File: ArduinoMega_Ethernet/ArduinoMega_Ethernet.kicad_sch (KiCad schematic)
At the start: 17 parts, among them SW1 RST_BTN, U1 ATmega2560-16A, Y1 16Mhz

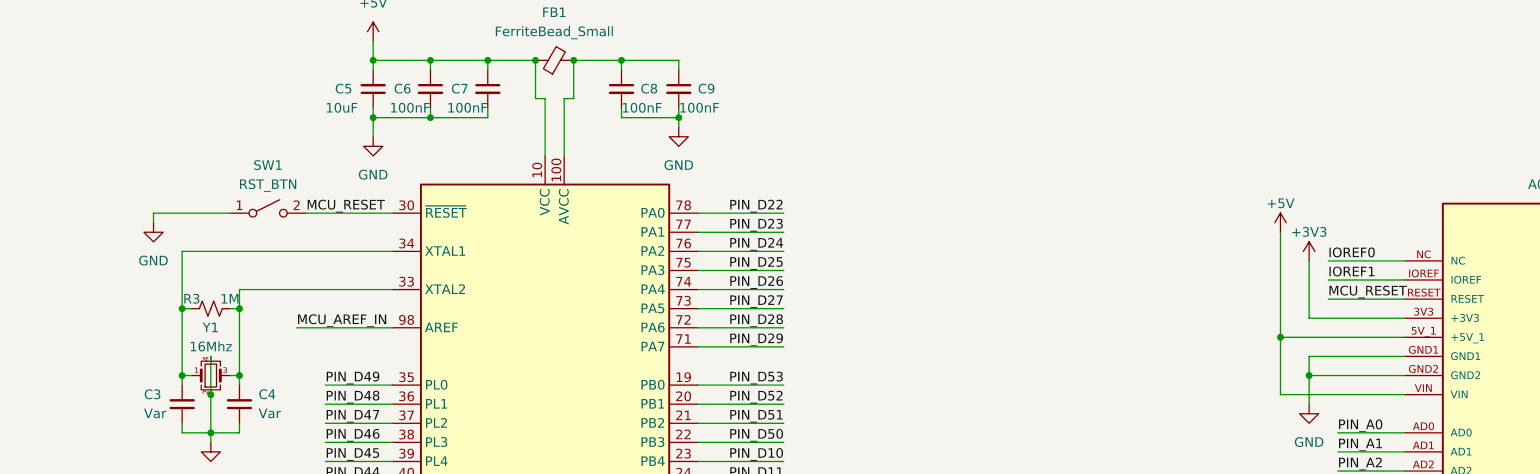
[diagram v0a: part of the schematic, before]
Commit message: add usb protection, fix ioref
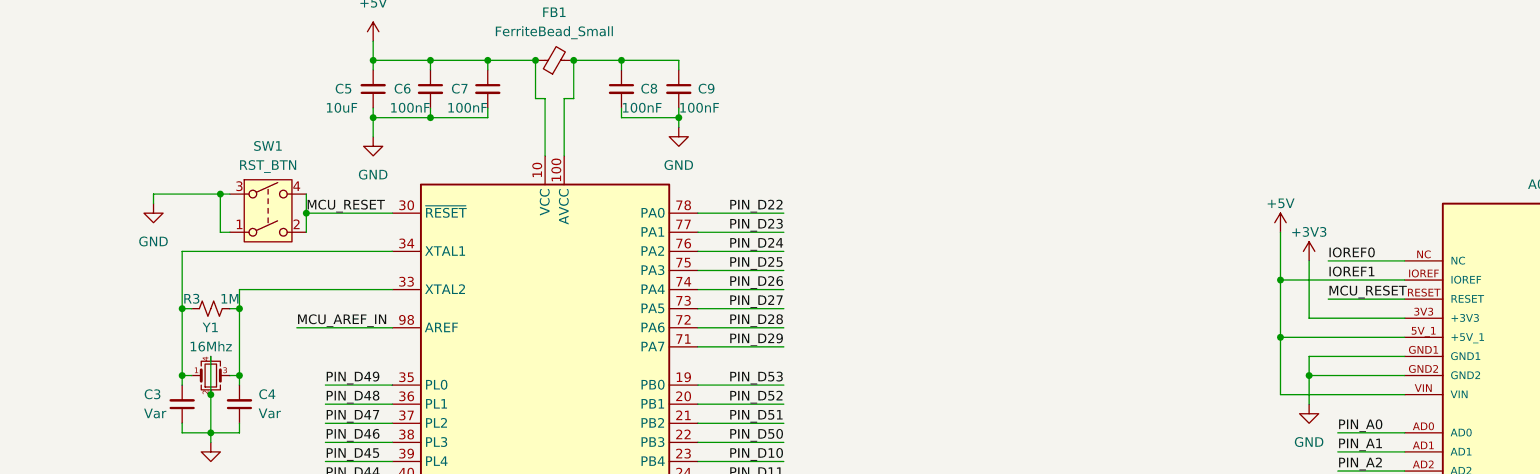
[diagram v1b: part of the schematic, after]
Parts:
- SW1: footprint Button_Switch_SMD:SW_Push_1P1T-MP_NO_Horizontal_Alps_SKRTLAE010 -> Button_Switch_SMD:SW_SPST_PTS645; symbol Switch:SW_SPST -> Switch:SW_DPST
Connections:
- net IOREF1 is gone; now on net +5V: A1.IOREF
- net GND: now also SW1.3
- net MCU_RESET: now also SW1.4

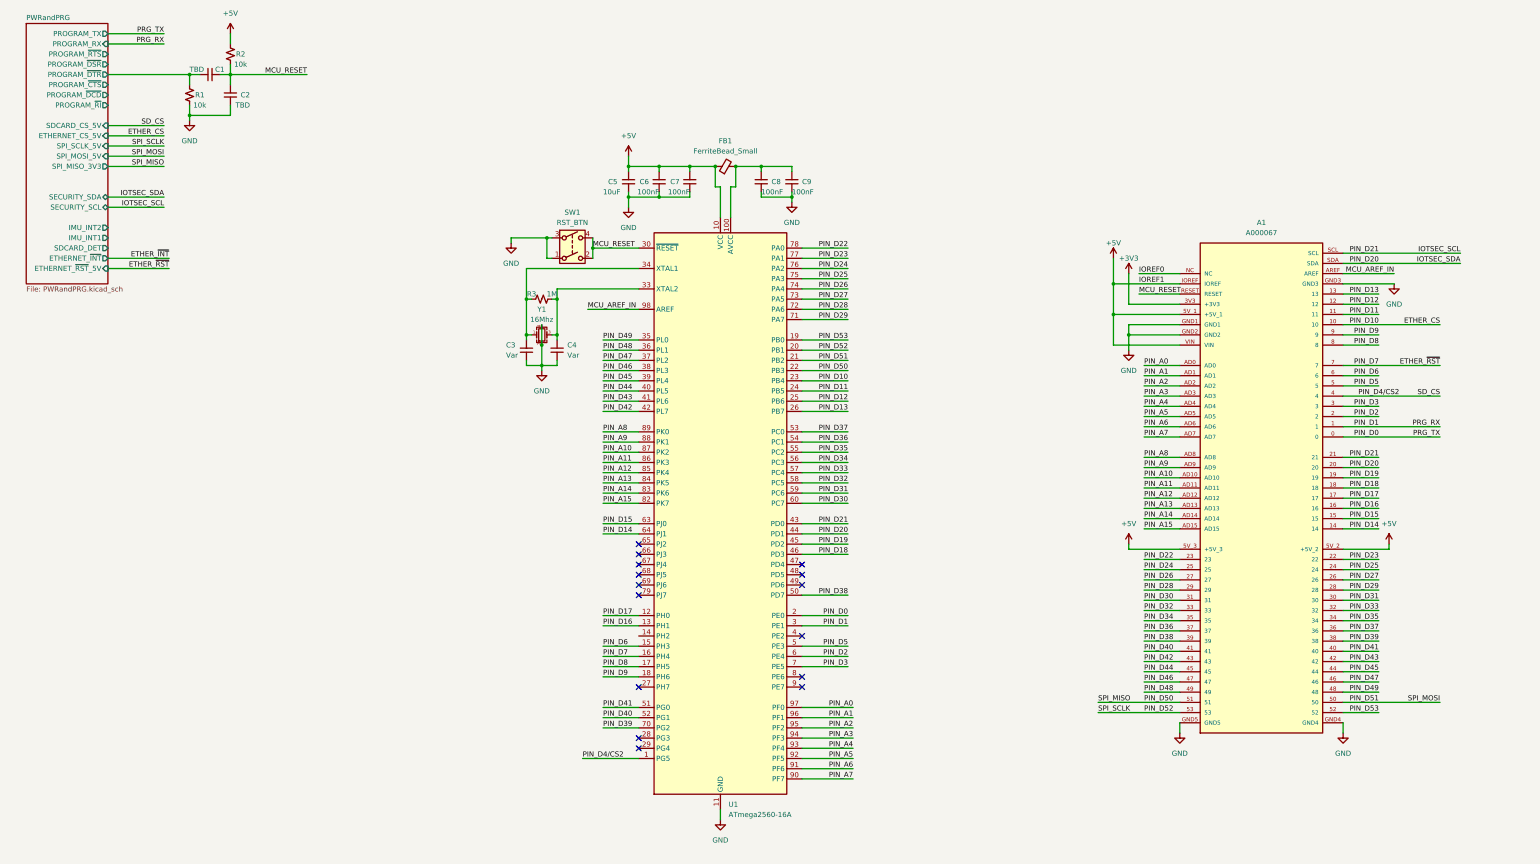
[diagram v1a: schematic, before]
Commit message: Fix IMU I2C, add SD Detect, Fix IoT CoPro Power
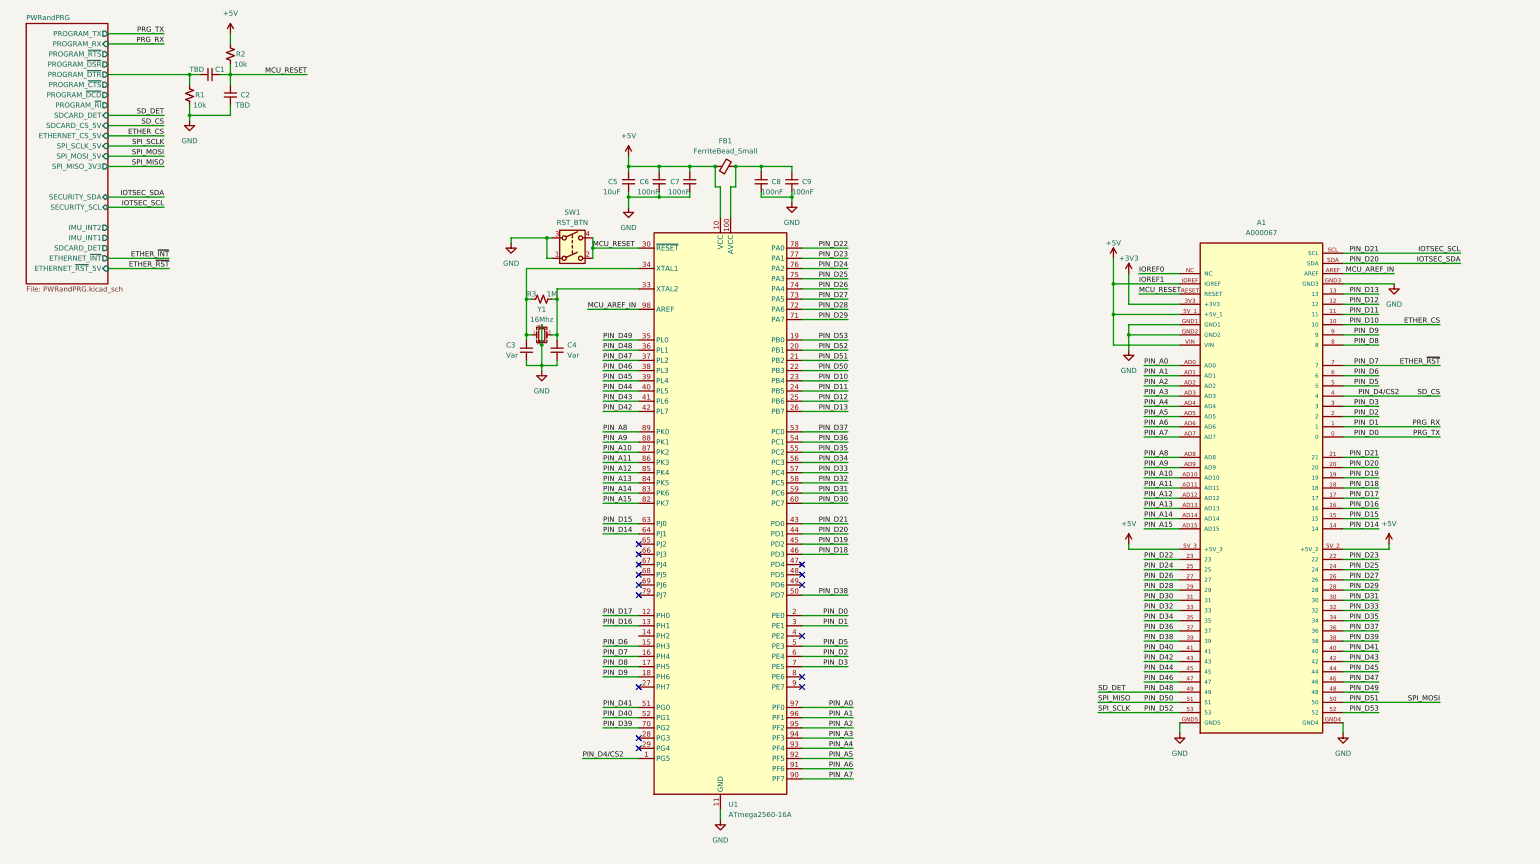
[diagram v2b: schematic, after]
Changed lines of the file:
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@@
 	(wire
 		(pts
+			(xy 283.21 186.69) (xy 303.53 186.69)
+		)
+		(stroke
+			(width 0)
+			(type default)
+		)
+	)
+	(wire
+		(pts
 			(xy 303.53 196.85) (xy 303.53 194.31)
 		)
@@
 	(wire
 		(pts
+			(xy 36.83 43.18) (xy 50.8 43.18)
+		)
+		(stroke
+			(width 0)
+			(type default)
+		)
+	)
+	(wire
+		(pts
 			(xy 157.48 76.2) (xy 157.48 78.74)
 		)
@@
 	(wire
 		(pts
-			(xy 294.64 186.69) (xy 303.53 186.69)
-		)
-		(stroke
-			(width 0)
-			(type default)
-		)
-	)
-	(wire
-		(pts
 			(xy 209.55 124.46) (xy 220.98 124.46)
 		)
@@
 		)
 	)
+	(label "SD_DET"
+		(at 50.8 43.18 180)
+		(effects
+			(font
+				(size 1.27 1.27)
+			)
+			(justify right bottom)
+		)
+	)
 	(label "PIN_D37"
 		(at 220.98 121.92 180)
@@
 		)
 	)
+	(label "SD_DET"
+		(at 283.21 186.69 0)
+		(effects
+			(font
+				(size 1.27 1.27)
+			)
+			(justify left bottom)
+		)
+	)
 	(label "PIN_A7"
 		(at 294.64 123.19 0)
@@
 			(effects
 				(font
+					(size 1.27 1.27)
+				)
+				(justify right)
+			)
+		)
+		(pin "SDCARD_DET" input
+			(at 36.83 43.18 0)
+			(effects
+				(font

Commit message: configurable io jumpers
configurable io jumpers
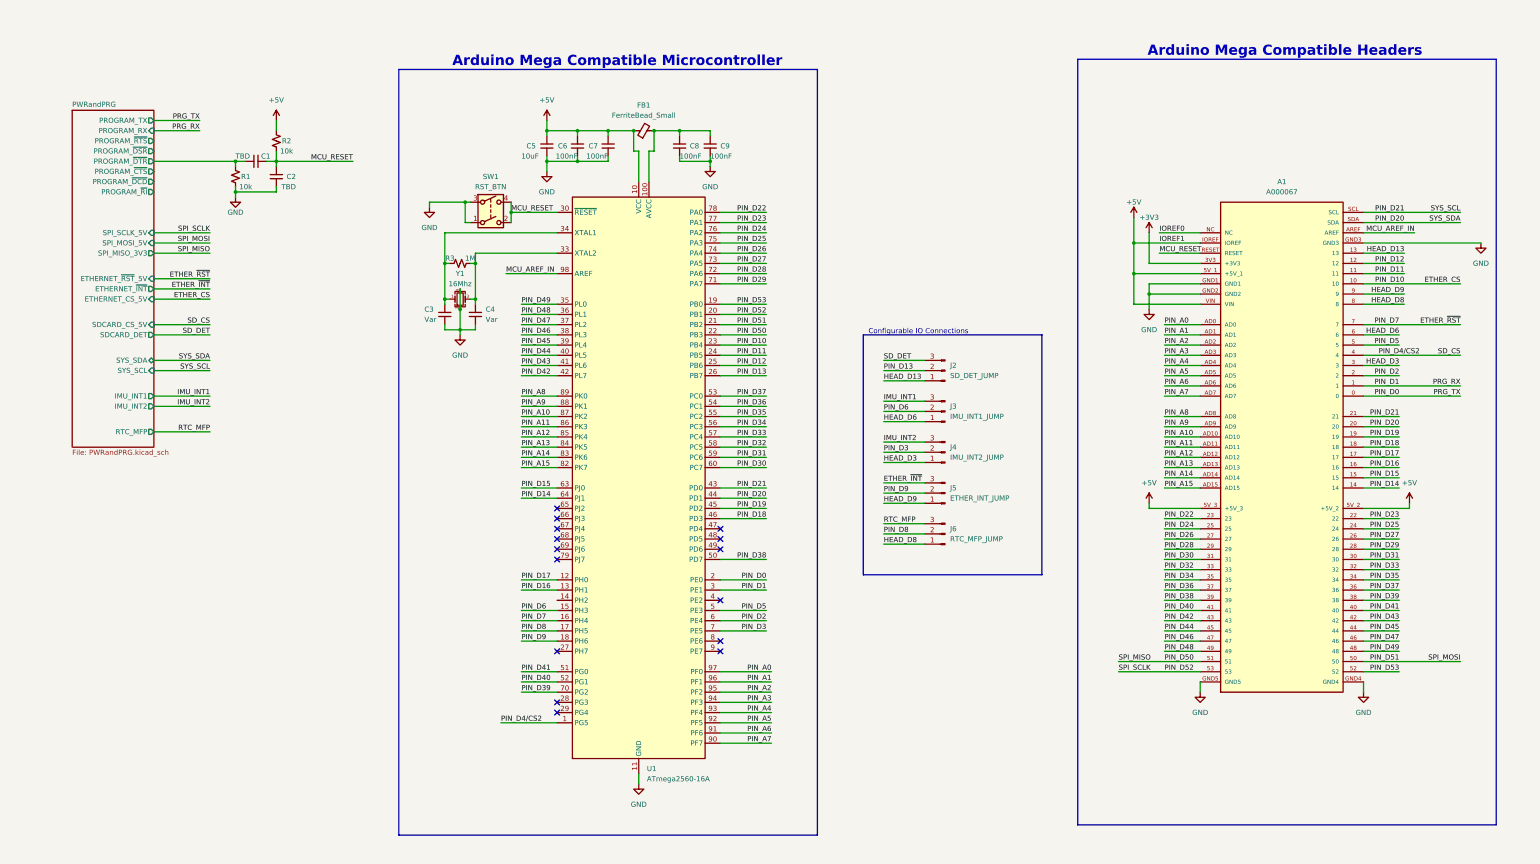
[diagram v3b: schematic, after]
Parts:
- added J2: SD_DET_JUMP, Connector_PinHeader_2.54mm:PinHeader_1x03_P2.54mm_Vertical, symbol Connector:Conn_01x03_Pin
- added J3: IMU_INT1_JUMP, Connector_PinHeader_2.54mm:PinHeader_1x03_P2.54mm_Vertical, symbol Connector:Conn_01x03_Pin
- added J4: IMU_INT2_JUMP, Connector_PinHeader_2.54mm:PinHeader_1x03_P2.54mm_Vertical, symbol Connector:Conn_01x03_Pin
- added J5: ETHER_INT_JUMP, Connector_PinHeader_2.54mm:PinHeader_1x03_P2.54mm_Vertical, symbol Connector:Conn_01x03_Pin
- added J6: RTC_MFP_JUMP, Connector_PinHeader_2.54mm:PinHeader_1x03_P2.54mm_Vertical, symbol Connector:Conn_01x03_Pin
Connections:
- net ETHER_~{INT}: now also J5.3 (Pin_3)
- net PIN_D13: now also J2.2 (Pin_2); no longer A1.13
- net PIN_D3: now also J4.2 (Pin_2); no longer A1.3
- net PIN_D6: now also J3.2 (Pin_2); no longer A1.6
- net PIN_D8: now also J6.2 (Pin_2); no longer A1.8
- net PIN_D9: now also J5.2 (Pin_2); no longer A1.9
- net IOTSEC_SCL renamed PIN_D21
- net IOTSEC_SDA renamed PIN_D20
- new net HEAD_D13: A1.13, J2.1 (Pin_1)
- new net HEAD_D3: A1.3, J4.1 (Pin_1)
- new net HEAD_D6: A1.6, J3.1 (Pin_1)
- new net HEAD_D8: A1.8, J6.1 (Pin_1)
- new net HEAD_D9: A1.9, J5.1 (Pin_1)
- new net IMU_INT1: J3.3 (Pin_3)
- new net IMU_INT2: J4.3 (Pin_3)
- new net RTC_MFP: J6.3 (Pin_3)
- new net SD_DET: J2.3 (Pin_3)
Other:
- sheet PWRandPRG ports: added RTC_MFP, SYS_SCL, SYS_SDA; removed SECURITY_SCL, SECURITY_SDA
- note added: "Arduino Mega Compatible Headers"
- note added: "Arduino Mega Compatible Microcontroller"
- note added: "Configurable IO Connections"
- title: MegaEtherBoard -> Ardunio Mega with Ethernet
- moved on the sheet: A1, C1, C2, C3, C4, C5, C6, C7, C8, C9, FB1, R1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

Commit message: I2C and Silkscreen revision
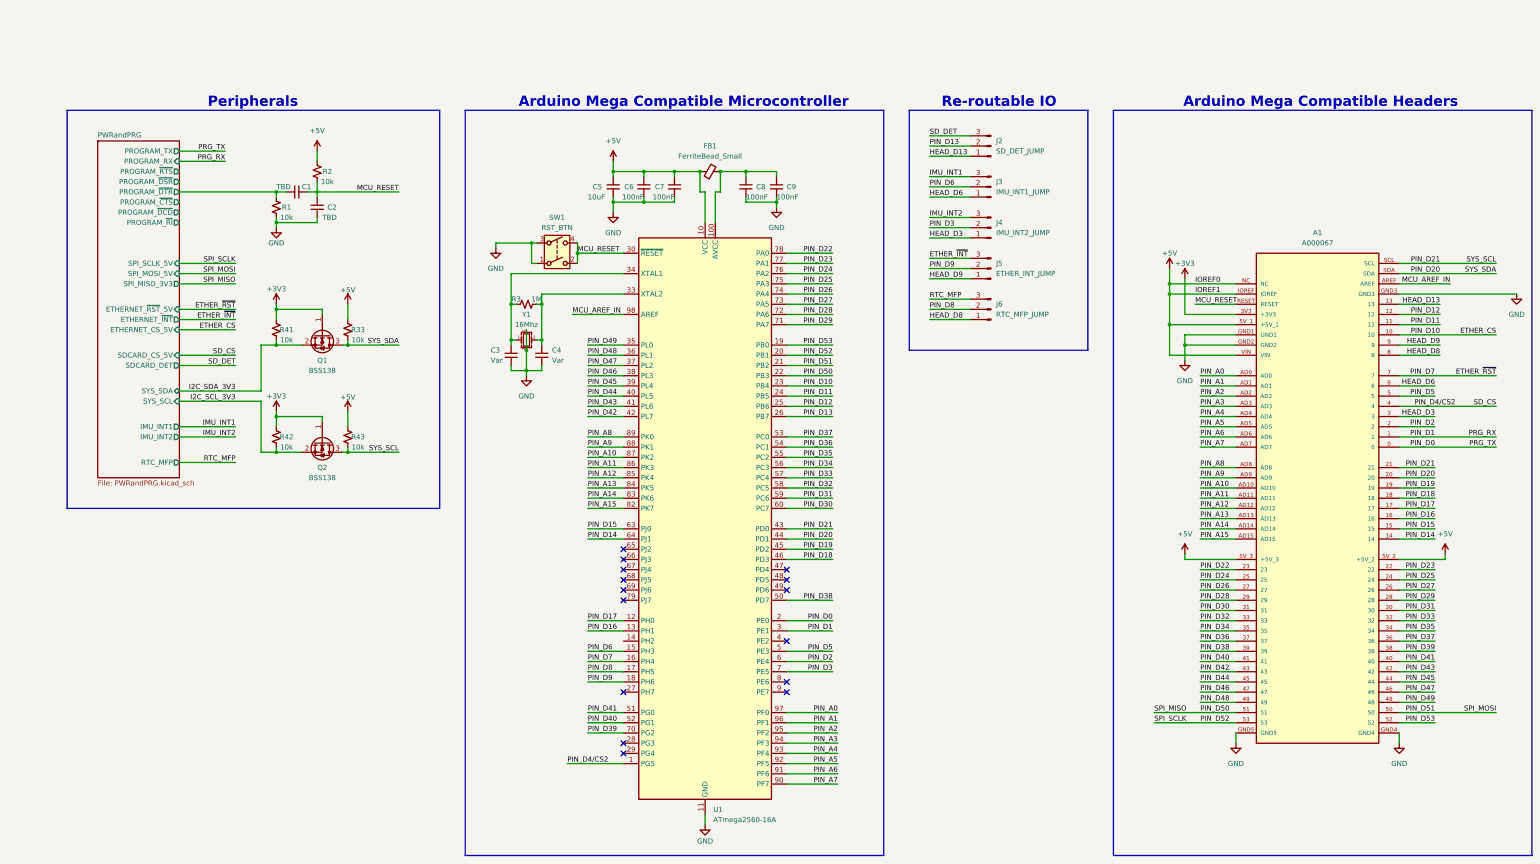
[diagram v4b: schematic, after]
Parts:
- added Q1, Q2: BSS138, Package_TO_SOT_SMD:SOT-23, symbol Transistor_FET:BSS138
- added R33, R41, R42, R43: 10k, Resistor_SMD:R_0603_1608Metric, symbol Device:R_Small_US
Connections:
- net IOREF0 is gone; now on net +5V: A1.NC
- net +3V3: now also Q1.1 (G), Q2.1 (G), R41.1, R42.1
- net +5V: now also R33.1, R43.1
- net PIN_D20: now also Q1.3 (D), R33.2
- net PIN_D21: now also Q2.3 (D), R43.2
- new net I2C_SCL_3V3: Q2.2 (S), R42.2
- new net I2C_SDA_3V3: Q1.2 (S), R41.2
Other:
- note added: "Peripherals"
- note added: "Re-routable IO"
- note removed: "Configurable IO Connections"
- moved on the sheet: A1, C1, C2, C3, C4, C5, C6, C7, C8, C9, FB1, J2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

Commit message: update level shifter, configurable pmode
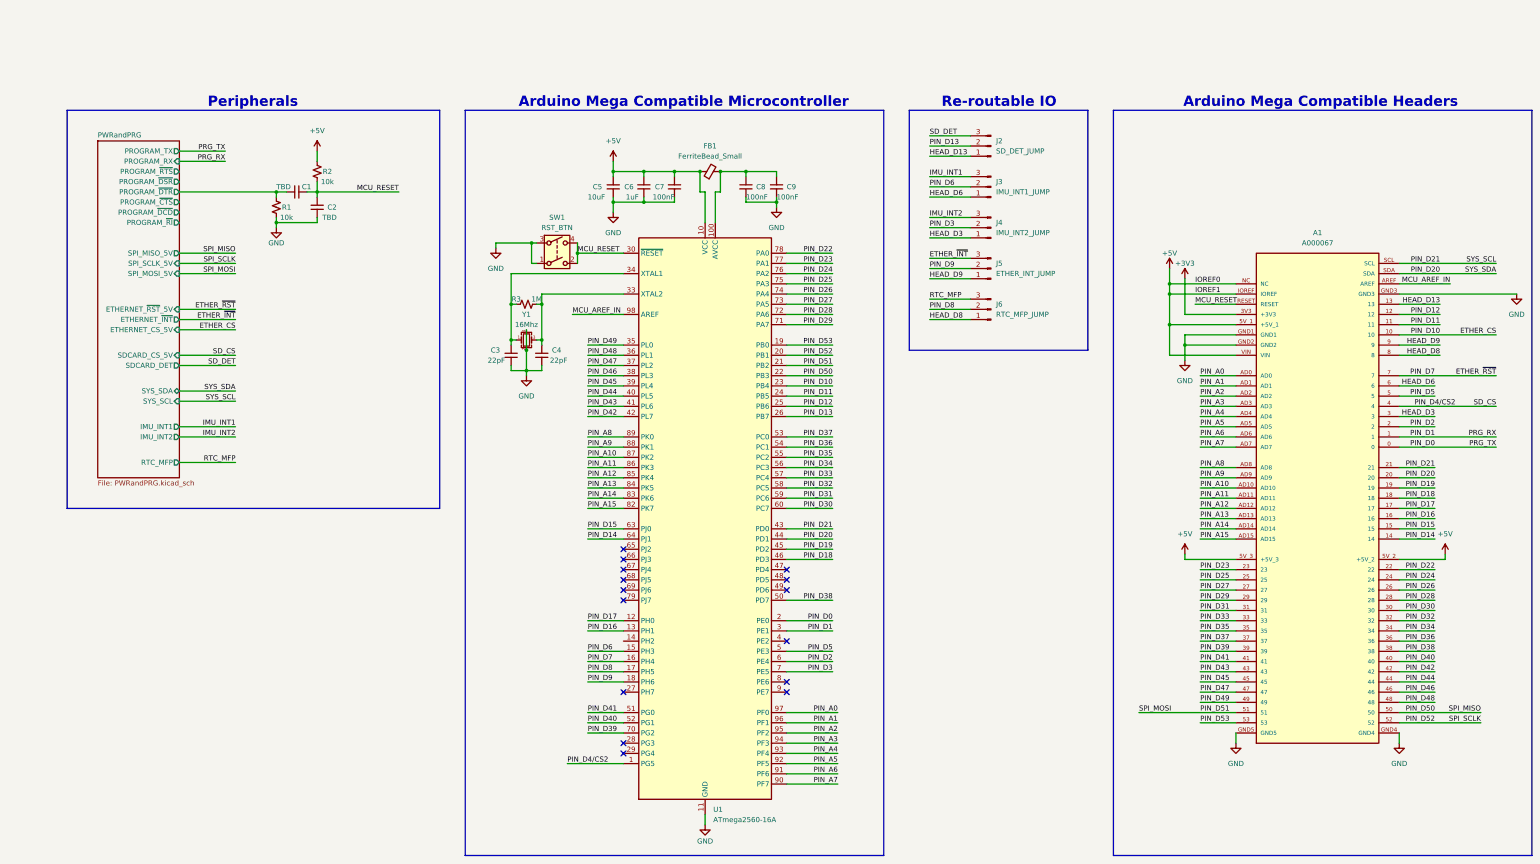
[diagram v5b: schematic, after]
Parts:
- removed Q1, Q2: BSS138, Package_TO_SOT_SMD:SOT-23, symbol Transistor_FET:BSS138
- removed R33, R41, R42, R43: 10k, Resistor_SMD:R_0603_1608Metric, symbol Device:R_Small_US
- A1: footprint footprints:ARDUINO_A000067 -> CUSTOM_PAD:ARDUINO_A000067
- C3, C4: value Var -> 22pF
- C6: value 100nF -> 1uF
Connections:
- net PIN_D22: now also A1.22; no longer A1.23
- net PIN_D23: now also A1.23; no longer A1.22
- net PIN_D24: now also A1.24; no longer A1.25
- net PIN_D25: now also A1.25; no longer A1.24
- net PIN_D26: now also A1.26; no longer A1.27
- net PIN_D27: now also A1.27; no longer A1.26
- net PIN_D28: now also A1.28; no longer A1.29
- net PIN_D29: now also A1.29; no longer A1.28
- net PIN_D30: now also A1.30; no longer A1.31
- net PIN_D31: now also A1.31; no longer A1.30
- net PIN_D32: now also A1.32; no longer A1.33
- net PIN_D33: now also A1.33; no longer A1.32
- net PIN_D34: now also A1.34; no longer A1.35
- net PIN_D35: now also A1.35; no longer A1.34
- net PIN_D36: now also A1.36; no longer A1.37
- net PIN_D37: now also A1.37; no longer A1.36
- net PIN_D38: now also A1.38; no longer A1.39
- net PIN_D39: now also A1.39; no longer A1.38
- net PIN_D40: now also A1.40; no longer A1.41
- net PIN_D41: now also A1.41; no longer A1.40
- net PIN_D42: now also A1.42; no longer A1.43
- net PIN_D43: now also A1.43; no longer A1.42
- net PIN_D44: now also A1.44; no longer A1.45
- net PIN_D45: now also A1.45; no longer A1.44
- net PIN_D46: now also A1.46; no longer A1.47
- net PIN_D47: now also A1.47; no longer A1.46
- net PIN_D48: now also A1.48; no longer A1.49
- net PIN_D49: now also A1.49; no longer A1.48
- net PIN_D50: now also A1.50; no longer A1.51
- net PIN_D51: now also A1.51; no longer A1.50
- net PIN_D52: now also A1.52; no longer A1.53
- net PIN_D53: now also A1.53; no longer A1.52
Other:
- sheet PWRandPRG ports: added SPI_MISO_5V; removed SPI_MISO_3V3

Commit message: Add files via upload
fix undersized capacitors
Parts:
- C5: footprint Capacitor_SMD:C_1206_3216Metric -> Capacitor_SMD:C_0805_2012Metric_Pad1.18x1.45mm_HandSolder
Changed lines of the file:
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@@
 			)
 		)
-		(property "Footprint" "Capacitor_SMD:C_1206_3216Metric"
+		(property "Footprint" "Capacitor_SMD:C_0805_2012Metric_Pad1.18x1.45mm_HandSolder"
 			(at 162.56 60.96 0)
 			(effects
